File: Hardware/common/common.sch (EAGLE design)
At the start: 24 parts, among them U1 788BS, U10 788BS, U11 788BS, U12 788BS, U13 788BS, U14 788BS, U15 788BS, U16 788BS, U2 788BS, U3 788BS, U4 788BS, U5 788BS, U6 788BS, U7 788BS, U8 788BS, U9 788BS

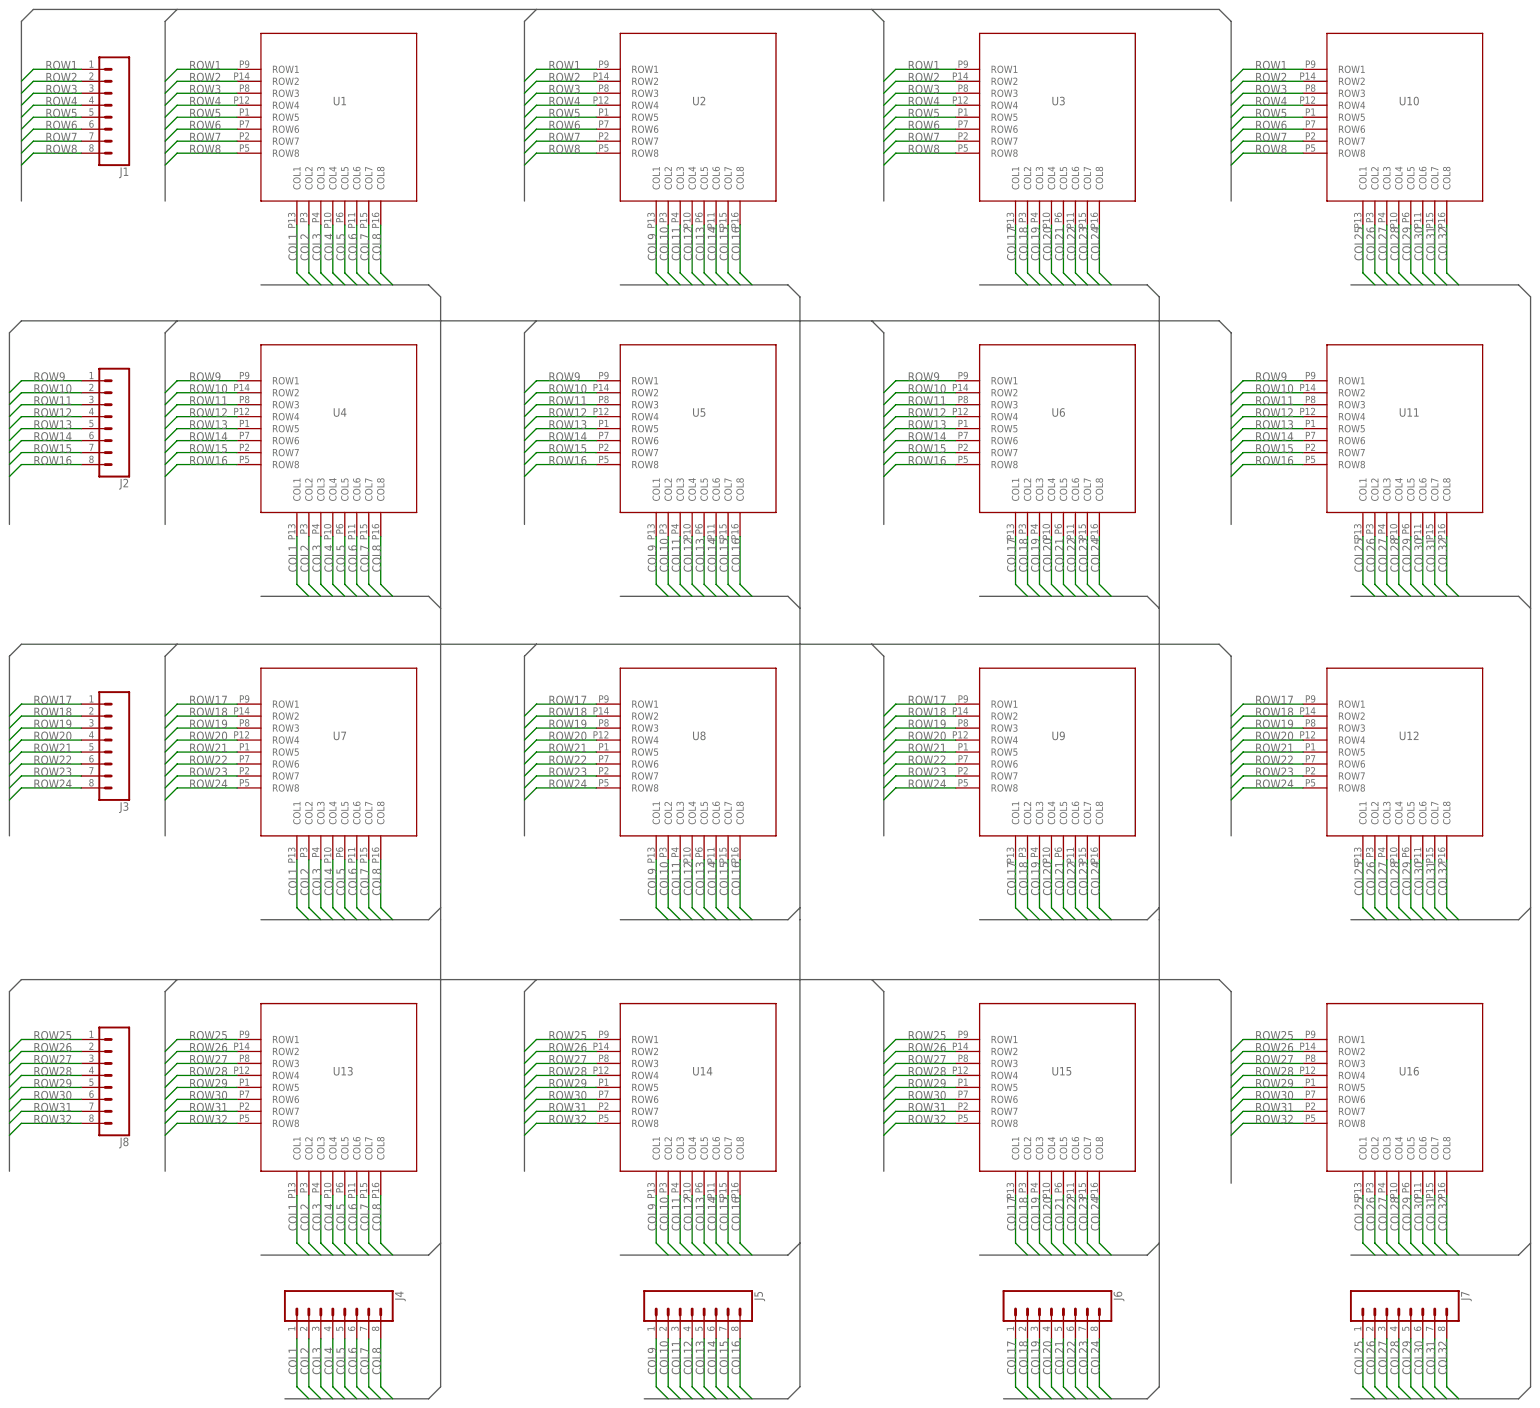
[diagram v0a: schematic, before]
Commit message: Got row/col reversed
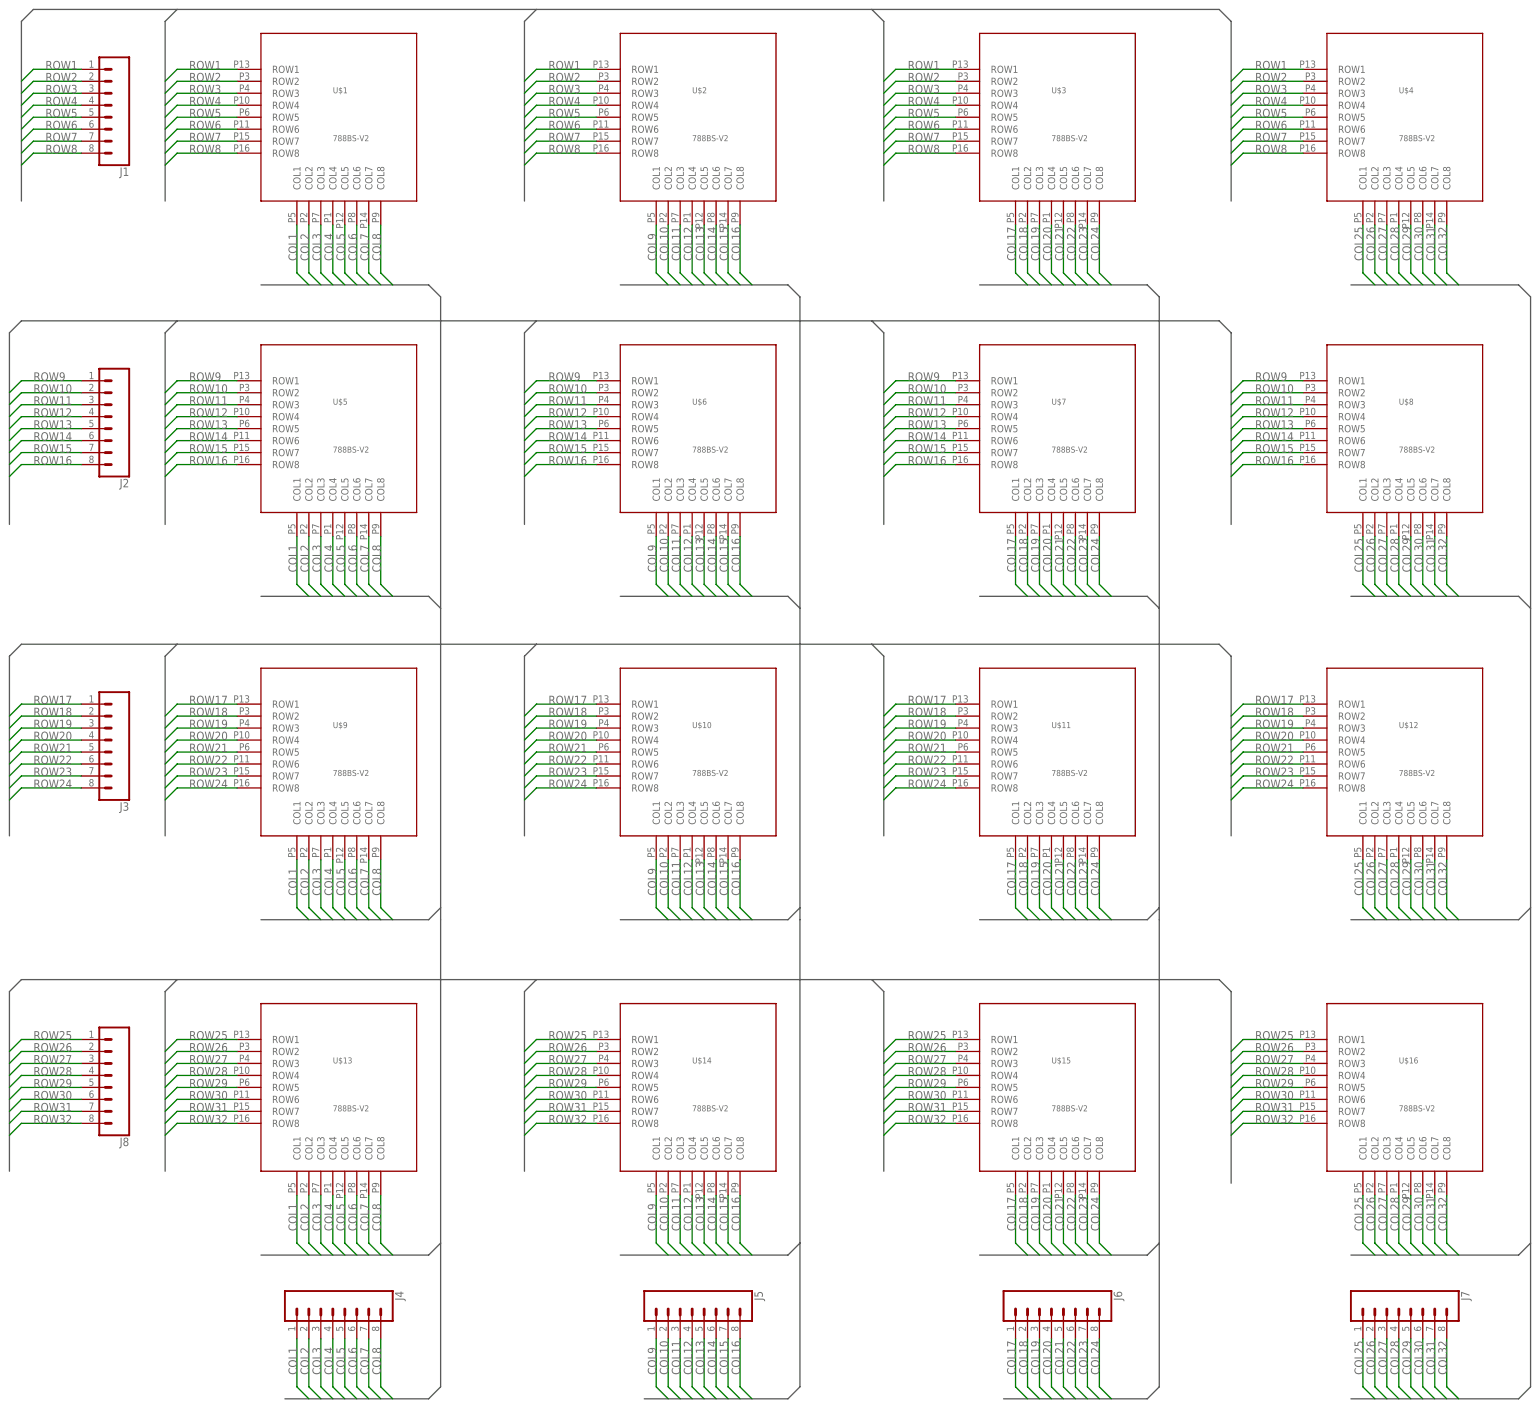
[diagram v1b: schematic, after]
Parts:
- removed U1, U10, U11, U12, U13, U14, U15, U16, U2, U3, U4, U5, U6, U7, U8, U9: 788BS, ledmatrix:788BS
- added U$1, U$10, U$11, U$12, U$13, U$14, U$15, U$16, U$2, U$3, U$4, U$5, U$6, U$7, U$8, U$9: 788BS-V2, ledmatrix-v2:788BS-V2
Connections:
- net COL1: now also U$1.COL1, U$13.COL1, U$5.COL1, U$9.COL1; no longer U1.COL1, U13.COL1, U4.COL1, U7.COL1
- net COL10: now also U$10.COL2, U$14.COL2, U$2.COL2, U$6.COL2; no longer U14.COL2, U2.COL2, U5.COL2, U8.COL2
- net COL11: now also U$10.COL3, U$14.COL3, U$2.COL3, U$6.COL3; no longer U14.COL3, U2.COL3, U5.COL3, U8.COL3
- net COL12: now also U$10.COL4, U$14.COL4, U$2.COL4, U$6.COL4; no longer U14.COL4, U2.COL4, U5.COL4, U8.COL4
- net COL13: now also U$10.COL5, U$14.COL5, U$2.COL5, U$6.COL5; no longer U14.COL5, U2.COL5, U5.COL5, U8.COL5
- net COL14: now also U$10.COL6, U$14.COL6, U$2.COL6, U$6.COL6; no longer U14.COL6, U2.COL6, U5.COL6, U8.COL6
- net COL15: now also U$10.COL7, U$14.COL7, U$2.COL7, U$6.COL7; no longer U14.COL7, U2.COL7, U5.COL7, U8.COL7
- net COL16: now also U$10.COL8, U$14.COL8, U$2.COL8, U$6.COL8; no longer U14.COL8, U2.COL8, U5.COL8, U8.COL8
- net COL17: now also U$11.COL1, U$15.COL1, U$3.COL1, U$7.COL1; no longer U15.COL1, U3.COL1, U6.COL1, U9.COL1
- net COL18: now also U$11.COL2, U$15.COL2, U$3.COL2, U$7.COL2; no longer U15.COL2, U3.COL2, U6.COL2, U9.COL2
- net COL19: now also U$11.COL3, U$15.COL3, U$3.COL3, U$7.COL3; no longer U15.COL3, U3.COL3, U6.COL3, U9.COL3
- net COL2: now also U$1.COL2, U$13.COL2, U$5.COL2, U$9.COL2; no longer U1.COL2, U13.COL2, U4.COL2, U7.COL2
- net COL20: now also U$11.COL4, U$15.COL4, U$3.COL4, U$7.COL4; no longer U15.COL4, U3.COL4, U6.COL4, U9.COL4
- net COL21: now also U$11.COL5, U$15.COL5, U$3.COL5, U$7.COL5; no longer U15.COL5, U3.COL5, U6.COL5, U9.COL5
- net COL22: now also U$11.COL6, U$15.COL6, U$3.COL6, U$7.COL6; no longer U15.COL6, U3.COL6, U6.COL6, U9.COL6
- net COL23: now also U$11.COL7, U$15.COL7, U$3.COL7, U$7.COL7; no longer U15.COL7, U3.COL7, U6.COL7, U9.COL7
- net COL24: now also U$11.COL8, U$15.COL8, U$3.COL8, U$7.COL8; no longer U15.COL8, U3.COL8, U6.COL8, U9.COL8
- net COL25: now also U$12.COL1, U$16.COL1, U$4.COL1, U$8.COL1; no longer U10.COL1, U11.COL1, U12.COL1, U16.COL1
- net COL26: now also U$12.COL2, U$16.COL2, U$4.COL2, U$8.COL2; no longer U10.COL2, U11.COL2, U12.COL2, U16.COL2
- net COL27: now also U$12.COL3, U$16.COL3, U$4.COL3, U$8.COL3; no longer U10.COL3, U11.COL3, U12.COL3, U16.COL3
- net COL28: now also U$12.COL4, U$16.COL4, U$4.COL4, U$8.COL4; no longer U10.COL4, U11.COL4, U12.COL4, U16.COL4
- net COL29: now also U$12.COL5, U$16.COL5, U$4.COL5, U$8.COL5; no longer U10.COL5, U11.COL5, U12.COL5, U16.COL5
- net COL3: now also U$1.COL3, U$13.COL3, U$5.COL3, U$9.COL3; no longer U1.COL3, U13.COL3, U4.COL3, U7.COL3
- net COL30: now also U$12.COL6, U$16.COL6, U$4.COL6, U$8.COL6; no longer U10.COL6, U11.COL6, U12.COL6, U16.COL6
- net COL31: now also U$12.COL7, U$16.COL7, U$4.COL7, U$8.COL7; no longer U10.COL7, U11.COL7, U12.COL7, U16.COL7
- net COL32: now also U$12.COL8, U$16.COL8, U$4.COL8, U$8.COL8; no longer U10.COL8, U11.COL8, U12.COL8, U16.COL8
- net COL4: now also U$1.COL4, U$13.COL4, U$5.COL4, U$9.COL4; no longer U1.COL4, U13.COL4, U4.COL4, U7.COL4
- net COL5: now also U$1.COL5, U$13.COL5, U$5.COL5, U$9.COL5; no longer U1.COL5, U13.COL5, U4.COL5, U7.COL5
- net COL6: now also U$1.COL6, U$13.COL6, U$5.COL6, U$9.COL6; no longer U1.COL6, U13.COL6, U4.COL6, U7.COL6
- net COL7: now also U$1.COL7, U$13.COL7, U$5.COL7, U$9.COL7; no longer U1.COL7, U13.COL7, U4.COL7, U7.COL7
- net COL8: now also U$1.COL8, U$13.COL8, U$5.COL8, U$9.COL8; no longer U1.COL8, U13.COL8, U4.COL8, U7.COL8
- net COL9: now also U$10.COL1, U$14.COL1, U$2.COL1, U$6.COL1; no longer U14.COL1, U2.COL1, U5.COL1, U8.COL1
- net ROW1: now also U$1.ROW1, U$2.ROW1, U$3.ROW1, U$4.ROW1; no longer U1.ROW1, U10.ROW1, U2.ROW1, U3.ROW1
- net ROW10: now also U$5.ROW2, U$6.ROW2, U$7.ROW2, U$8.ROW2; no longer U11.ROW2, U4.ROW2, U5.ROW2, U6.ROW2
- net ROW11: now also U$5.ROW3, U$6.ROW3, U$7.ROW3, U$8.ROW3; no longer U11.ROW3, U4.ROW3, U5.ROW3, U6.ROW3
- net ROW12: now also U$5.ROW4, U$6.ROW4, U$7.ROW4, U$8.ROW4; no longer U11.ROW4, U4.ROW4, U5.ROW4, U6.ROW4
- net ROW13: now also U$5.ROW5, U$6.ROW5, U$7.ROW5, U$8.ROW5; no longer U11.ROW5, U4.ROW5, U5.ROW5, U6.ROW5
- net ROW14: now also U$5.ROW6, U$6.ROW6, U$7.ROW6, U$8.ROW6; no longer U11.ROW6, U4.ROW6, U5.ROW6, U6.ROW6
- net ROW15: now also U$5.ROW7, U$6.ROW7, U$7.ROW7, U$8.ROW7; no longer U11.ROW7, U4.ROW7, U5.ROW7, U6.ROW7
- net ROW16: now also U$5.ROW8, U$6.ROW8, U$7.ROW8, U$8.ROW8; no longer U11.ROW8, U4.ROW8, U5.ROW8, U6.ROW8
- net ROW17: now also U$10.ROW1, U$11.ROW1, U$12.ROW1, U$9.ROW1; no longer U12.ROW1, U7.ROW1, U8.ROW1, U9.ROW1
- net ROW18: now also U$10.ROW2, U$11.ROW2, U$12.ROW2, U$9.ROW2; no longer U12.ROW2, U7.ROW2, U8.ROW2, U9.ROW2
- net ROW19: now also U$10.ROW3, U$11.ROW3, U$12.ROW3, U$9.ROW3; no longer U12.ROW3, U7.ROW3, U8.ROW3, U9.ROW3
- net ROW2: now also U$1.ROW2, U$2.ROW2, U$3.ROW2, U$4.ROW2; no longer U1.ROW2, U10.ROW2, U2.ROW2, U3.ROW2
- net ROW20: now also U$10.ROW4, U$11.ROW4, U$12.ROW4, U$9.ROW4; no longer U12.ROW4, U7.ROW4, U8.ROW4, U9.ROW4
- net ROW21: now also U$10.ROW5, U$11.ROW5, U$12.ROW5, U$9.ROW5; no longer U12.ROW5, U7.ROW5, U8.ROW5, U9.ROW5
- net ROW22: now also U$10.ROW6, U$11.ROW6, U$12.ROW6, U$9.ROW6; no longer U12.ROW6, U7.ROW6, U8.ROW6, U9.ROW6
- net ROW23: now also U$10.ROW7, U$11.ROW7, U$12.ROW7, U$9.ROW7; no longer U12.ROW7, U7.ROW7, U8.ROW7, U9.ROW7
- net ROW24: now also U$10.ROW8, U$11.ROW8, U$12.ROW8, U$9.ROW8; no longer U12.ROW8, U7.ROW8, U8.ROW8, U9.ROW8
- net ROW25: now also U$13.ROW1, U$14.ROW1, U$15.ROW1, U$16.ROW1; no longer U13.ROW1, U14.ROW1, U15.ROW1, U16.ROW1
- net ROW26: now also U$13.ROW2, U$14.ROW2, U$15.ROW2, U$16.ROW2; no longer U13.ROW2, U14.ROW2, U15.ROW2, U16.ROW2
- net ROW27: now also U$13.ROW3, U$14.ROW3, U$15.ROW3, U$16.ROW3; no longer U13.ROW3, U14.ROW3, U15.ROW3, U16.ROW3
- net ROW28: now also U$13.ROW4, U$14.ROW4, U$15.ROW4, U$16.ROW4; no longer U13.ROW4, U14.ROW4, U15.ROW4, U16.ROW4
- net ROW29: now also U$13.ROW5, U$14.ROW5, U$15.ROW5, U$16.ROW5; no longer U13.ROW5, U14.ROW5, U15.ROW5, U16.ROW5
- net ROW3: now also U$1.ROW3, U$2.ROW3, U$3.ROW3, U$4.ROW3; no longer U1.ROW3, U10.ROW3, U2.ROW3, U3.ROW3
- net ROW30: now also U$13.ROW6, U$14.ROW6, U$15.ROW6, U$16.ROW6; no longer U13.ROW6, U14.ROW6, U15.ROW6, U16.ROW6
- net ROW31: now also U$13.ROW7, U$14.ROW7, U$15.ROW7, U$16.ROW7; no longer U13.ROW7, U14.ROW7, U15.ROW7, U16.ROW7
- net ROW32: now also U$13.ROW8, U$14.ROW8, U$15.ROW8, U$16.ROW8; no longer U13.ROW8, U14.ROW8, U15.ROW8, U16.ROW8
- net ROW4: now also U$1.ROW4, U$2.ROW4, U$3.ROW4, U$4.ROW4; no longer U1.ROW4, U10.ROW4, U2.ROW4, U3.ROW4
- net ROW5: now also U$1.ROW5, U$2.ROW5, U$3.ROW5, U$4.ROW5; no longer U1.ROW5, U10.ROW5, U2.ROW5, U3.ROW5
- net ROW6: now also U$1.ROW6, U$2.ROW6, U$3.ROW6, U$4.ROW6; no longer U1.ROW6, U10.ROW6, U2.ROW6, U3.ROW6
- net ROW7: now also U$1.ROW7, U$2.ROW7, U$3.ROW7, U$4.ROW7; no longer U1.ROW7, U10.ROW7, U2.ROW7, U3.ROW7
- net ROW8: now also U$1.ROW8, U$2.ROW8, U$3.ROW8, U$4.ROW8; no longer U1.ROW8, U10.ROW8, U2.ROW8, U3.ROW8
- net ROW9: now also U$5.ROW1, U$6.ROW1, U$7.ROW1, U$8.ROW1; no longer U11.ROW1, U4.ROW1, U5.ROW1, U6.ROW1
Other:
- note removed: "U1"
- note removed: "U10"
- note removed: "U11"
- note removed: "U12"
- note removed: "U13"
- note removed: "U14"
- note removed: "U15"
- note removed: "U16"
- note removed: "U2"
- note removed: "U3"
- note removed: "U4"
- note removed: "U5"
- note removed: "U6"
- note removed: "U7"
- note removed: "U8"
- note removed: "U9"
